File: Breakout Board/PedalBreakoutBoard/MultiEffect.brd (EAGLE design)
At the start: 65.7 x 66 mm, 55 parts, among them IC1 LD1117V, IC2 MCP6004P, U1 OPA1652AID

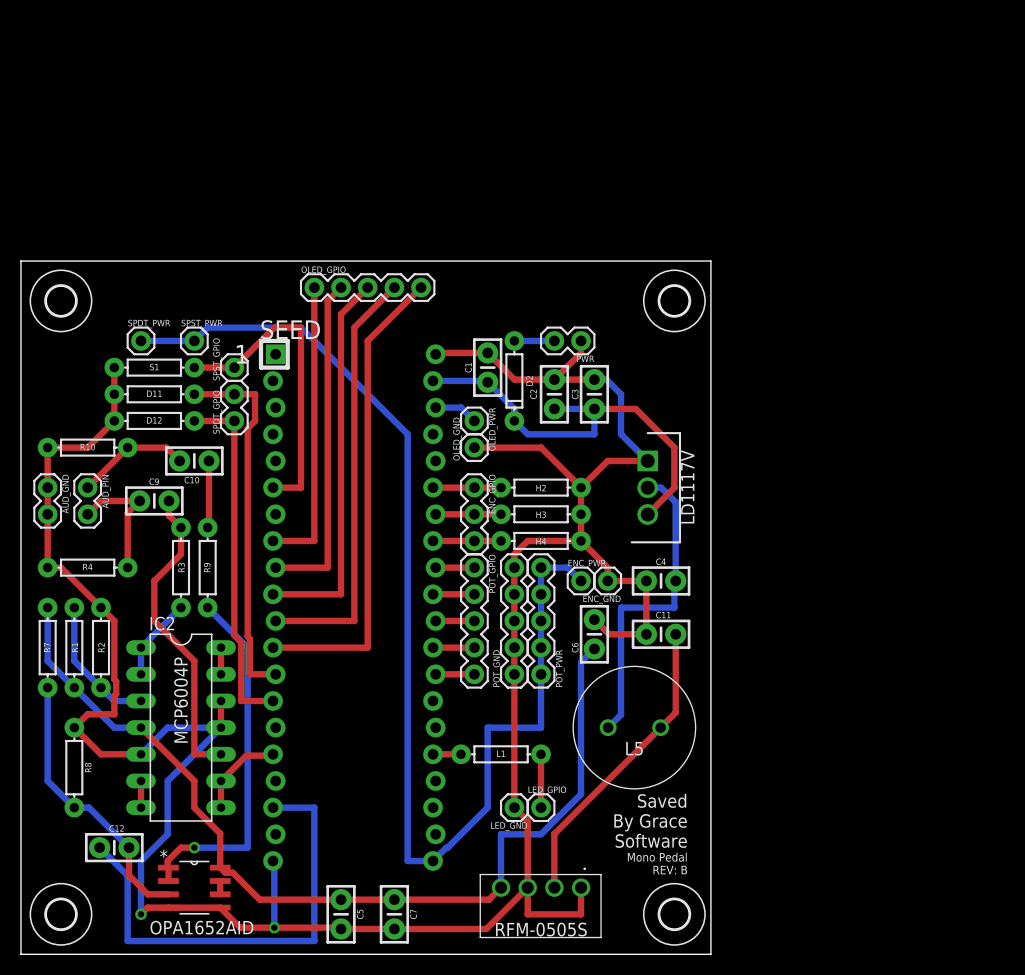
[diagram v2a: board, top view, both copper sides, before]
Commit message: DP-6 - Add additional LEDs
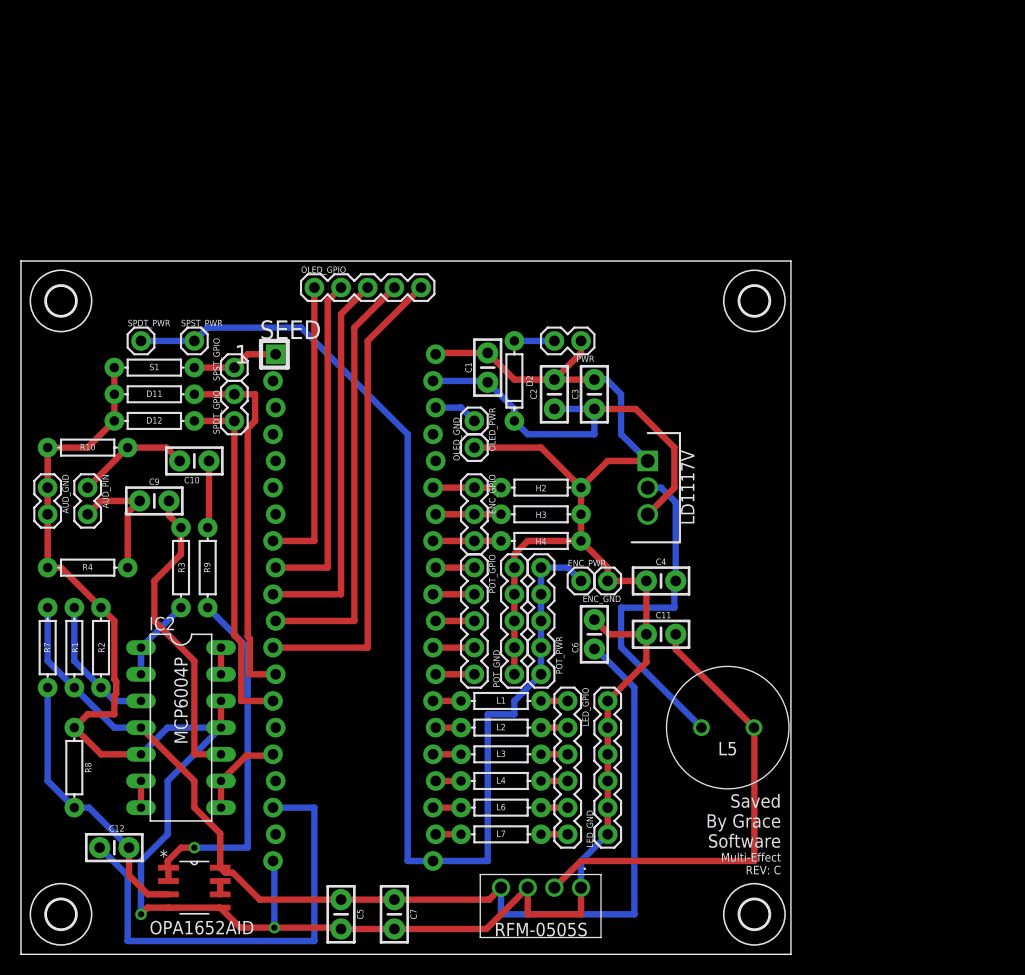
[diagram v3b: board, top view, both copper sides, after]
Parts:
- added L2, L3, L4, L6, L7: 330, SparkFun-Resistors:AXIAL-0.3
- LED_GND, LED_GPIO: device SparkFun-Connectors:1X01 -> SparkFun-Connectors:1X06
- moved LED_GPIO 10.5 mm to (52.1, 24.1), turned to 270 degrees
- moved LED_GND 9.25 mm to (55.9, 11.4), turned to 90 degrees
- moved L5 8.89 mm to (67.3, 21.6)
- moved H6 7.62 mm to (69.8, 62.2)
- moved H7 7.62 mm to (69.8, 3.81)
- moved L1 5.08 mm to (45.7, 24.1)
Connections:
- new net LED2: L2.P$1, SEED.26
- new net LED3: L3.P$1, SEED.25
- new net LED4: L4.P$1, SEED.24
- new net LED5: L6.P$1, SEED.23
- new net LED6: L7.P$1, SEED.22
- new net N$11: L6.P$2, LED_GPIO.5
- new net N$16: L7.P$2, LED_GPIO.6
- new net N$3: L2.P$2, LED_GPIO.2
- new net N$4: L3.P$2, LED_GPIO.3
- new net N$5: L4.P$2, LED_GPIO.4
- new net SPST2: SEED.2
- new net SPST3: SEED.3
- new net SPST4: SEED.4
- new net SPST5: SEED.5
- new net SPST6: SEED.6
- net GND: now also LED_GND.2, LED_GND.3, LED_GND.4, LED_GND.5, LED_GND.6
- net LED1: now also SEED.27; no longer SEED.25
- net SPST1: now also SEED.1; no longer SEED.6
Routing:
- net SPST1: track 29.6 -> 8.27 mm
- net N$7: track 28.9 -> 44.8 mm
- net +5V_ISOL: track 90.2 -> 103.7 mm
- net GND: track 255.4 -> 261.3 mm
- net LED5: track 0.00 -> 2.67 mm
- net LED3: track 0.00 -> 2.67 mm
- net N$8: track 30.3 -> 33.0 mm
- net N$1: track 5.08 -> 2.54 mm
- net N$5: track 0.00 -> 2.54 mm
- net N$4: track 0.00 -> 2.54 mm
- net N$3: track 0.00 -> 2.54 mm
- net N$16: track 0.00 -> 2.54 mm
- net N$11: track 0.00 -> 2.54 mm
- net LED6: track 0.00 -> 2.41 mm
- net LED4: track 0.00 -> 2.41 mm
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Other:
- board size 65.7 x 66 mm -> 73.3 x 66 mm
- board text added: "Multi-Effect REV: C"
- board text removed: "Mono Pedal REV: B"

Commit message: DP-6 - Re-layout of audio noise reduction circuit
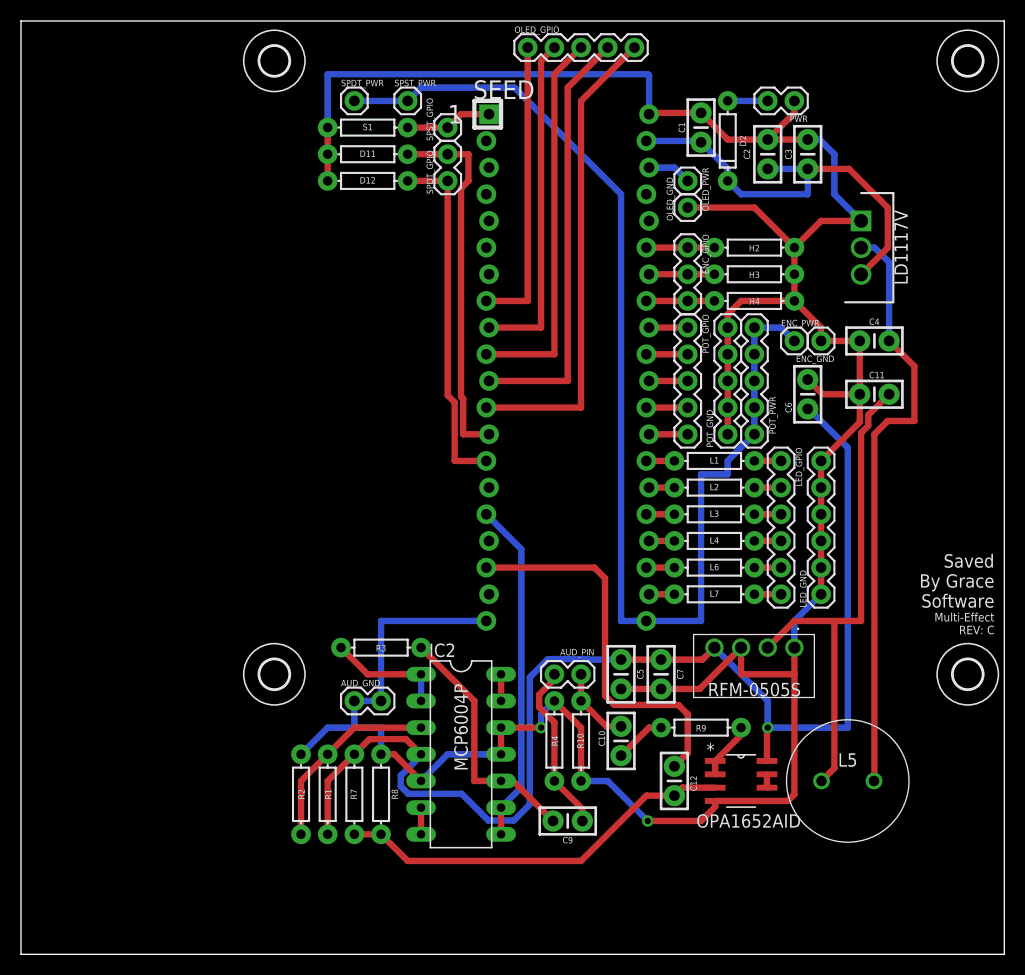
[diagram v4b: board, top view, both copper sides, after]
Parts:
- moved R10 54.7 mm to (53.3, 20.3), turned to 90 degrees
- moved C12 53.7 mm to (62.2, 16.5), turned to 270 degrees
- moved U1 53.1 mm to (68.6, 16.5)
- moved AUD_PIN 50.2 mm to (53.3, 26.7), turned to 180 degrees
- moved C9 49.8 mm to (52.1, 12.7), turned to 180 degrees
- moved R9 49.4 mm to (64.8, 21.6), turned to 180 degrees
- moved C10 48.6 mm to (57.1, 20.3), turned to 90 degrees
- moved R4 47.4 mm to (50.8, 20.3), turned to 270 degrees
- moved AUD_GND 35.6 mm to (31.8, 24.1), turned to 0 degrees
- moved C5 35.1 mm to (57.1, 26.7)
- moved C7 34.2 mm to (61.0, 26.7)
- moved R7 32.4 mm to (31.8, 15.2)
- moved C6 30.6 mm to (74.9, 53.3)
- moved H6 30.6 mm to (90.2, 85.1)
- moved H7 30.6 mm to (90.2, 26.7)
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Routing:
- net N$13: track 34.5 -> 5.47 mm, vias 1 -> 0
- net GND: track 261.3 -> 287.9 mm
- net IN_L: track 8.62 -> 32.7 mm
- net N$8: track 33.0 -> 56.7 mm
- net +5V_ISOL: track 103.7 -> 117.8 mm, vias 0 -> 1
- net N$12: track 26.4 -> 38.3 mm
- net OUT_L: track 44.4 -> 37.0 mm
- net N$9: track 29.8 -> 23.9 mm
- net N$6: track 13.0 -> 18.6 mm
- net IN_L_JACK: track 12.3 -> 16.3 mm
- net N$7: track 44.8 -> 48.4 mm
- net OUT_L_JACK: track 10.9 -> 7.35 mm
- net V_AUDIOBIAS: track 7.93 -> 11.2 mm
- net N$14: track 6.40 -> 4.91 mm
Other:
- board size 73.3 x 66 mm -> 93.7 x 88.9 mm

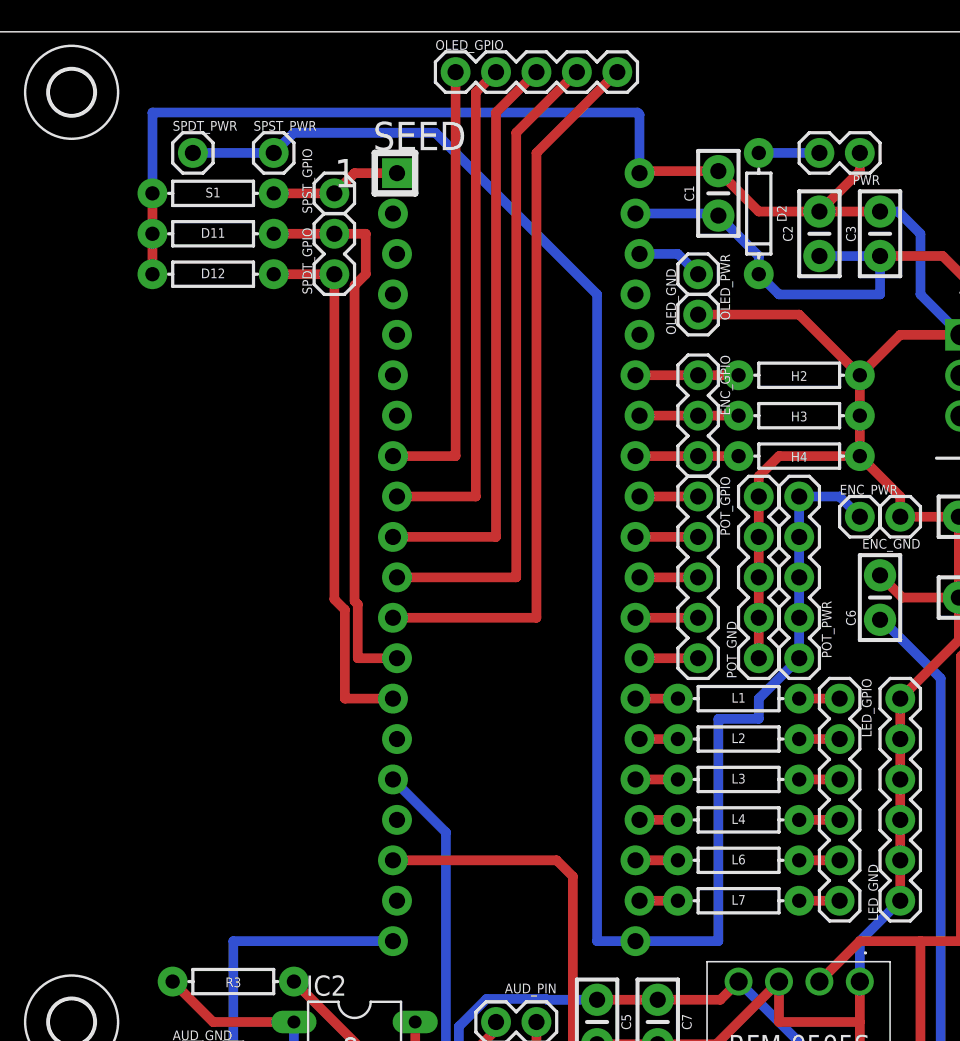
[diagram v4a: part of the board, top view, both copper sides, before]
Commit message: DP-6 - Add additional SPST connections
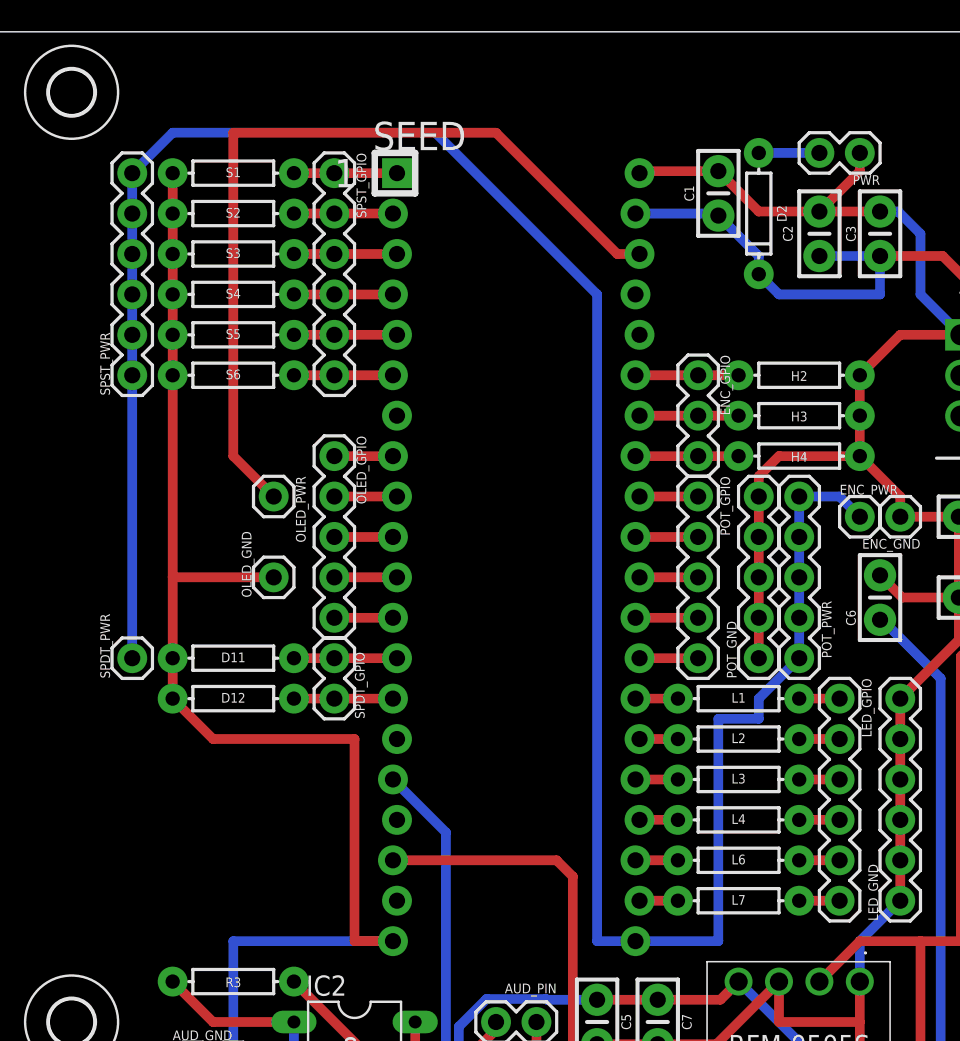
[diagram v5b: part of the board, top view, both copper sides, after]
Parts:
- added S2, S3, S4, S5, S6: 10k, SparkFun-Resistors:AXIAL-0.3
- SPST_GPIO, SPST_PWR: device SparkFun-Connectors:1X01 -> SparkFun-Connectors:1X06
- moved SPDT_PWR 32.0 mm to (27.9, 49.5), turned to 90 degrees
- moved OLED_GND 31.4 mm to (36.8, 54.6)
- moved OLED_PWR 30.1 mm to (36.8, 59.7)
- moved D11 26.7 mm to (34.3, 49.5)
- moved D12 26.7 mm to (34.3, 47.0)
- moved SPDT_GPIO 26.7 mm to (40.6, 47.0)
- moved OLED_GPIO 25.3 mm to (40.6, 62.2), turned to 270 degrees
- moved SPST_PWR 16.6 mm to (27.9, 67.3), turned to 90 degrees
- moved S1 1.80 mm to (34.3, 80.0)
- moved SPST_GPIO 1.27 mm to (40.6, 80.0), turned to 270 degrees
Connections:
- net +3V3_A: now also SPST_PWR.2, SPST_PWR.3, SPST_PWR.4, SPST_PWR.5, SPST_PWR.6
- net GND: now also S2.P$1, S3.P$1, S4.P$1, S5.P$1, S6.P$1
- net SPST2: now also S2.P$2, SPST_GPIO.2
- net SPST3: now also S3.P$2, SPST_GPIO.3
- net SPST4: now also S4.P$2, SPST_GPIO.4
- net SPST5: now also S5.P$2, SPST_GPIO.5
- net SPST6: now also S6.P$2, SPST_GPIO.6
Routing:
- net +3V3_D: track 4.21 -> 52.6 mm
- net RES: track 45.4 -> 3.68 mm
- net SDA: track 40.8 -> 3.94 mm
- net +3V3_A: track 114.3 -> 149.1 mm
- net DC: track 36.7 -> 3.68 mm
- net SPDT1_1: track 35.3 -> 6.48 mm
- net SCL: track 32.1 -> 3.94 mm
- net SPDT1_2: track 33.8 -> 6.22 mm
- net CS: track 28.1 -> 3.68 mm
- net GND: track 287.9 -> 298.6 mm
- net SPST5: track 0.00 -> 6.48 mm
- net SPST3: track 0.00 -> 6.48 mm
- net SPST6: track 0.00 -> 6.22 mm
- net SPST4: track 0.00 -> 6.22 mm
- net SPST2: track 0.00 -> 6.22 mm
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
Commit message: DP-6 - Board cleanup
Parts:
- moved H7 39.1 mm to (58.4, 3.81)
- moved H6 31.9 mm to (58.4, 82.5)
- moved H5 30.6 mm to (3.81, 3.81)
- moved C3 24.3 mm to (50.8, 73.7)
- moved C6 24.3 mm to (50.8, 50.8)
- moved L2 24.3 mm to (41.9, 41.9)
- moved L1 24.3 mm to (41.9, 44.5)
- moved L3 24.3 mm to (41.9, 39.4)
- moved L4 24.3 mm to (41.9, 36.8)
- moved L6 24.3 mm to (41.9, 34.3)
- moved L7 24.3 mm to (41.9, 31.8)
- moved AUD_PIN 24.3 mm to (29.2, 24.1)
- moved C11 24.3 mm to (57.1, 50.8)
- moved C2 24.3 mm to (47.0, 73.7)
- moved C7 24.3 mm to (36.8, 24.1)
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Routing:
- net N$2: track 3.81 -> 15.0 mm
- net GND: track 298.6 -> 300.8 mm
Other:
- board size 93.7 x 88.9 mm -> 61.9 x 86.3 mm
- board text added: "Multi-Effect Pedal REV: C"
- board text removed: "Multi-Effect REV: C"
